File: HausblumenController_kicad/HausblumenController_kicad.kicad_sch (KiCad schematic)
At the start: 19 parts, among them Q1 IRF520N, Q2 IRF520N, Q3 IRF520N, Q4 IRLML0030, SW1 RotaryEncoder_Switch_MP, U1 BlackPill_40pin_SWD, U2 DS18B20, U3 DHT11

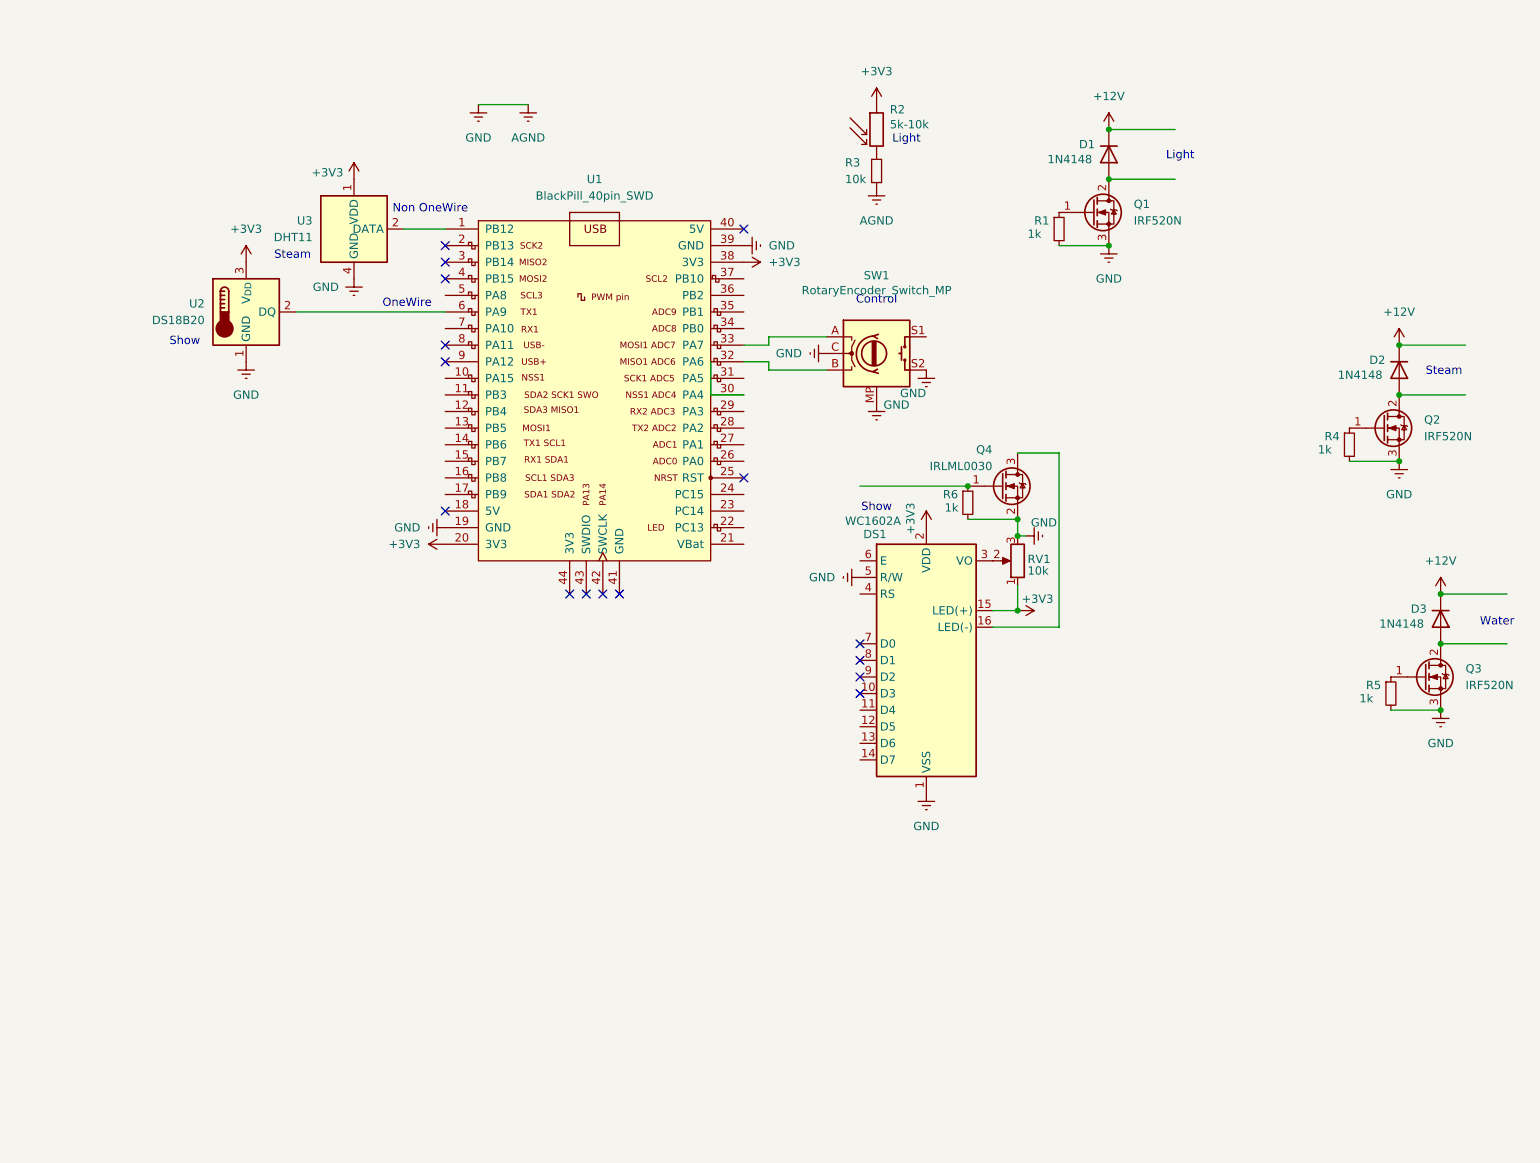
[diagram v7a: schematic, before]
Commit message: feat: added BME280 on schemes
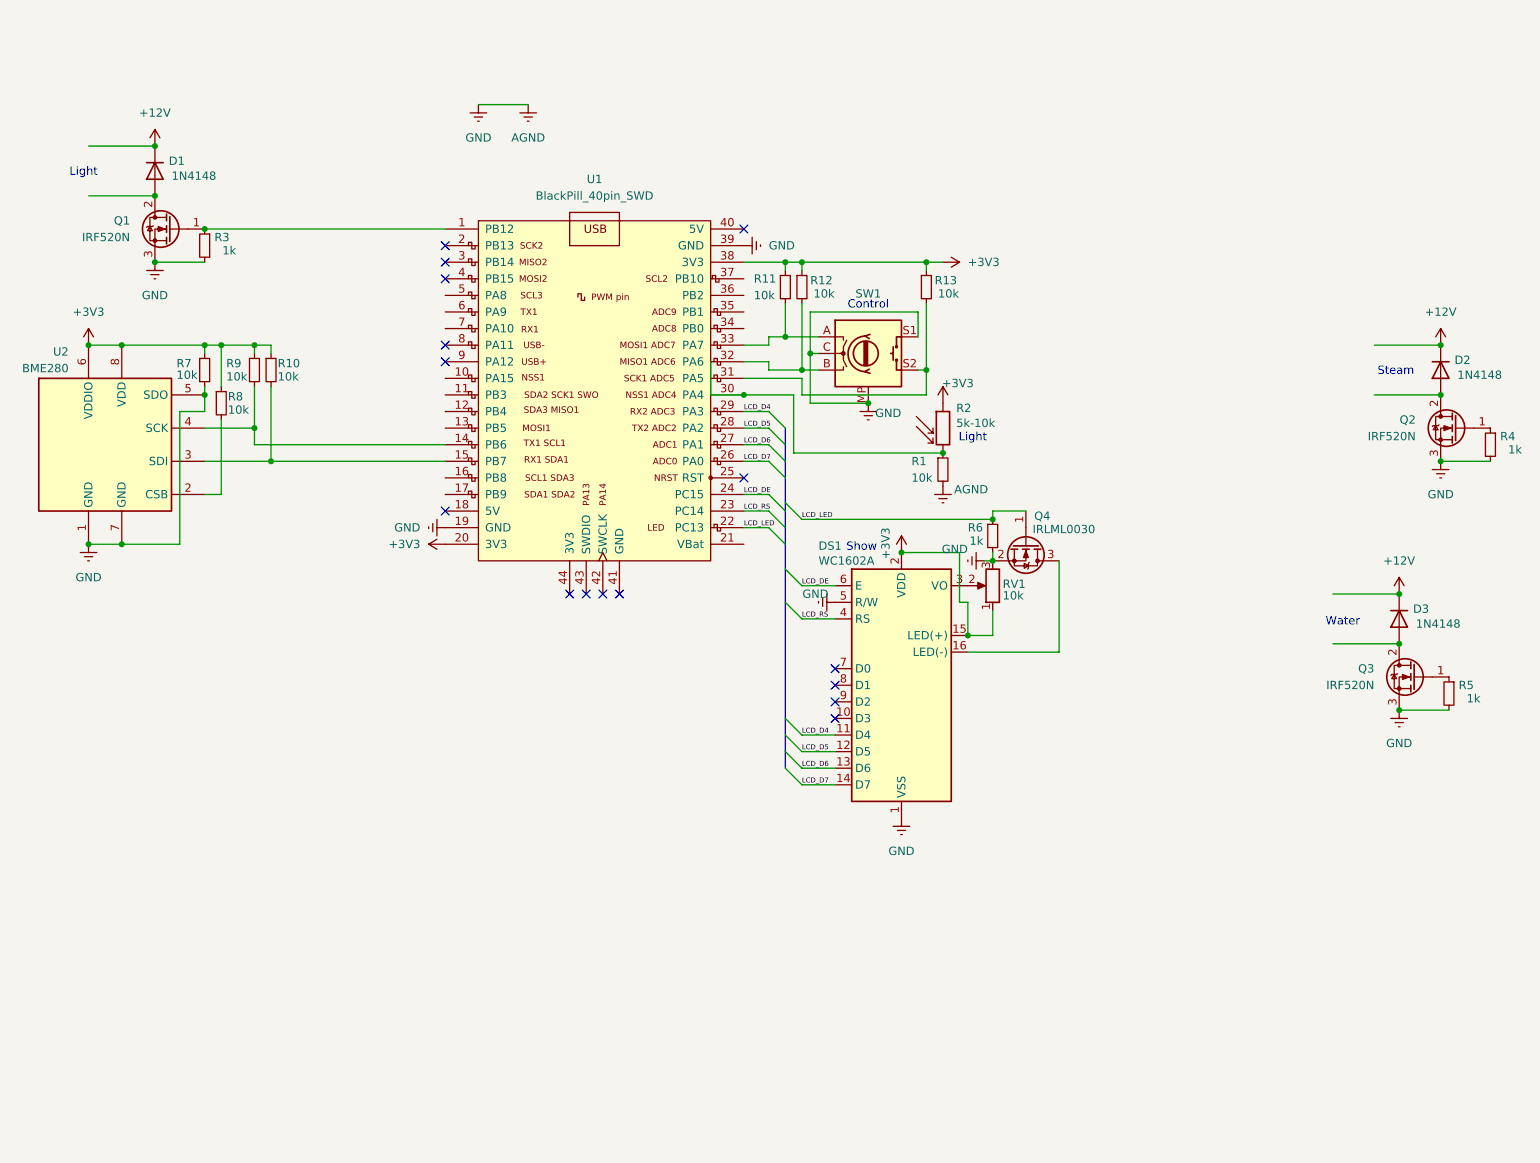
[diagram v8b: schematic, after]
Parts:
- removed U2: DS18B20, Package_TO_SOT_THT:TO-92_Inline, symbol Sensor_Temperature:DS18B20
- removed U3: DHT11, Sensor:Aosong_DHT11_5.5x12.0_P2.54mm, symbol Sensor:DHT11
- added R10, R11, R12, R13, R7, R8, R9: 10k, Resistor_SMD:R_0603_1608Metric, symbol Device:R_Small
- added U2: BME280, Package_LGA:Bosch_LGA-8_2.5x2.5mm_P0.65mm_ClockwisePinNumbering, symbol Sensor:BME280
- renumbered R3 to R1, R1 to R3
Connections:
- net +3V3: now also R10.1, R11.1, R12.1, R13.1, R7.1, R8.1, R9.1, U2.6 (VDDIO), U2.8 (VDD)
- net AGND: now also SW1.S1, R7.2, U2.1 (GND), U2.5 (SDO), U2.7 (GND); no longer SW1.S2
- net LCD_LED: now reaches Q4.1 (G), R6.1
- net LCD_LED: now also U1.22 (PC13)
- net at U1.1 (PB12): now also Q1.1 (G), R3.1
- net at U1.14 (PB6): now also R9.2, U2.4 (SCK)
- net at U1.15 (PB7): now also R10.2, U2.3 (SDI)
- net LCD_RS: now reaches U1.23 (PC14)
- net LCD_RS: now also DS1.4 (RS)
- net LCD_DE: now reaches U1.24 (PC15)
- net LCD_DE: now also DS1.6 (E)
- net LCD_D7: now reaches U1.26 (PA0)
- net LCD_D7: now also DS1.14 (D7)
- net LCD_D6: now reaches U1.27 (PA1)
- net LCD_D6: now also DS1.13 (D6)
- net LCD_D5: now reaches U1.28 (PA2)
- net LCD_D5: now also DS1.12 (D5)
- net LCD_D4: now reaches U1.29 (PA3)
- net LCD_D4: now also DS1.11 (D4)
- net at U1.30 (PA4): now also R1.1, R2.2
- net at U1.31 (PA5): now also SW1.S2, R13.2
- net at SW1.B, U1.32 (PA6): now also R12.2
- net at SW1.A, U1.33 (PA7): now also R11.2
- new net: R8.2, U2.2 (CSB)
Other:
- note removed: "Non OneWire"
- note removed: "OneWire"
- moved on the sheet: D1, D2, D3, DS1, Q1, Q2, Q3, Q4, R1, R2, R3, R4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
